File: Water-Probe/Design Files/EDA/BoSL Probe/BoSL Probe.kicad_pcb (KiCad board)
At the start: 2 copper layers, 25.4 x 12 mm, 9 parts, among them J1 8P8C_Shielded, U1 MS5803-01BA, U2 DS18B20

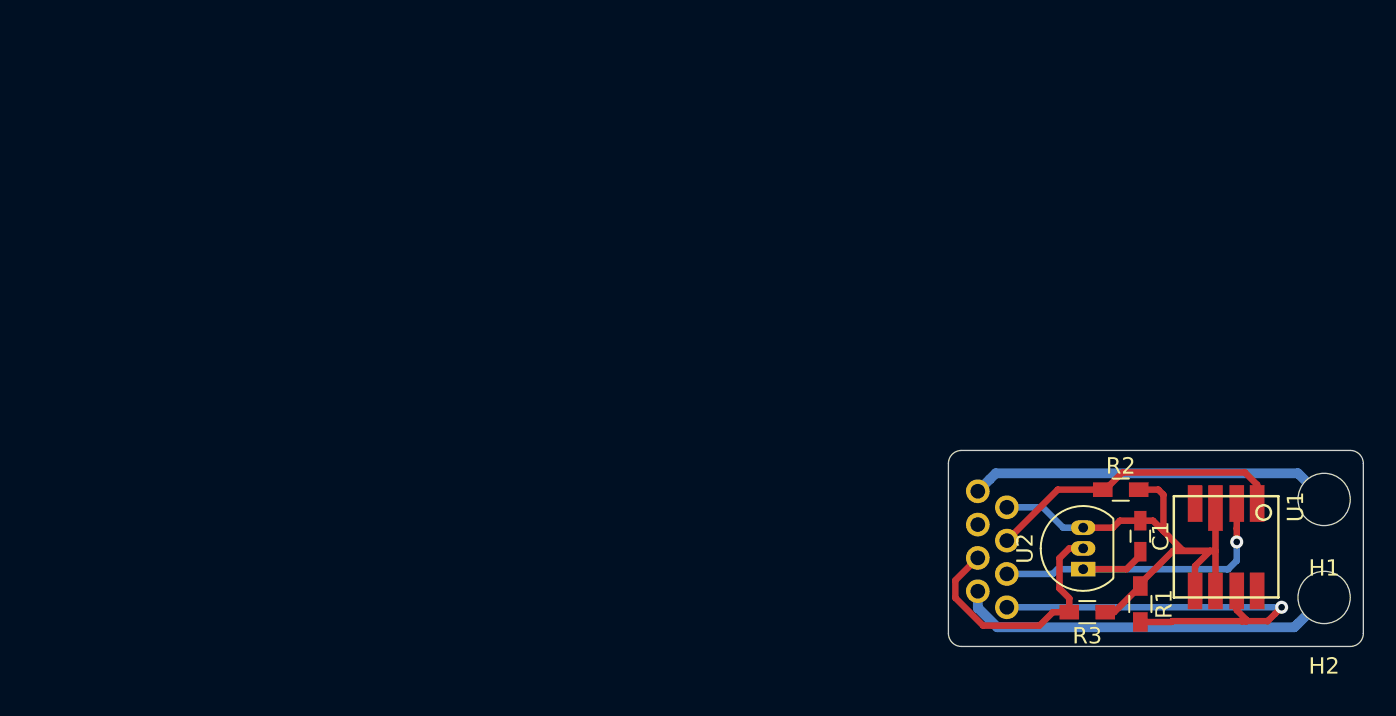
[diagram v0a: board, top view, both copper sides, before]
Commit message: finished modeling probe shape
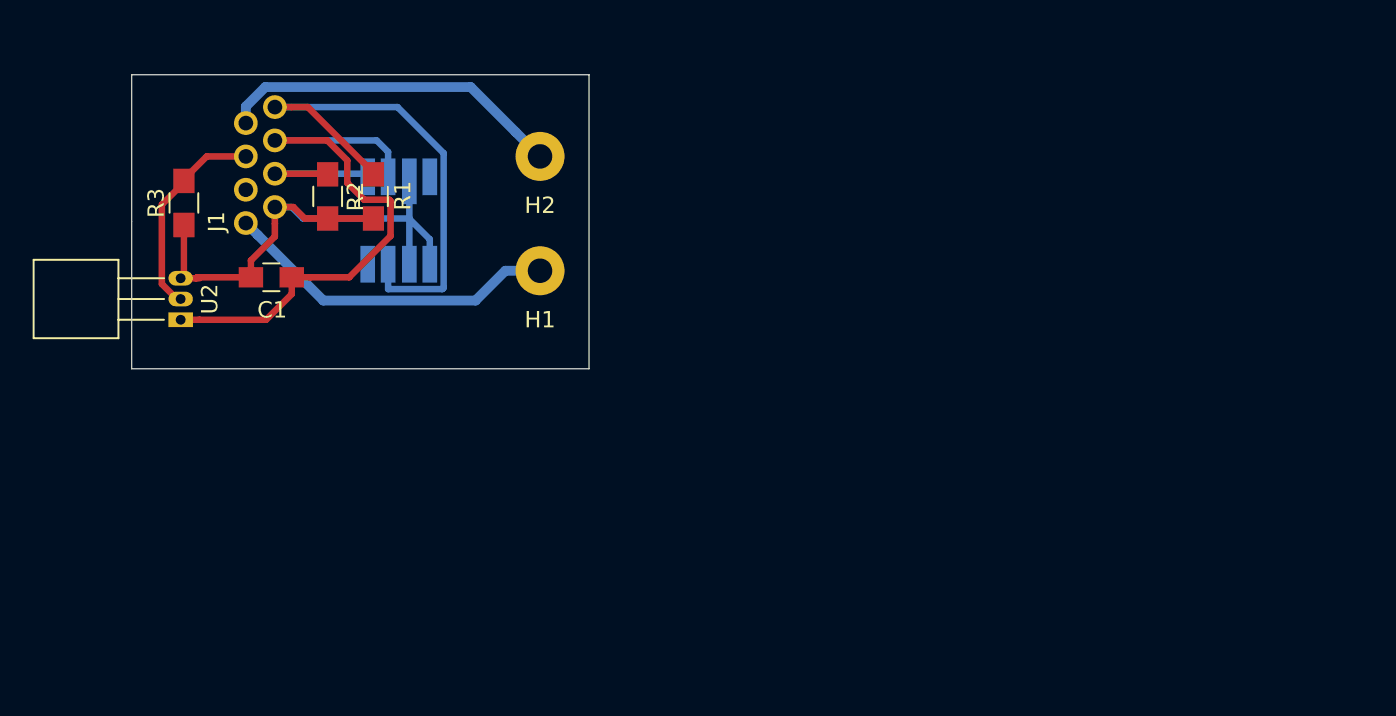
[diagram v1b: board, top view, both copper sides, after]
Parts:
- C1: footprint Capacitors_SMD:C_0603_HandSoldering -> Capacitors_SMD:C_0805_HandSoldering
- H1, H2: footprint Mounting_Holes:MountingHole_3.2mm_M3 -> Measurement_Points:Measurement_Point_Round-TH_Big
- J1: moved to F.Cu
- R1, R2, R3: footprint Resistors_SMD:R_0603_HandSoldering -> Resistors_SMD:R_0805_HandSoldering
- U1: moved to B.Cu
- U2: footprint TO_SOT_Packages_THT:TO-92_Inline_Narrow_Oval -> TO_SOT_Packages_THT:TO-92_Horizontal2_Inline_Narrow_Oval
- moved R3 60.7 mm to (103.2, 98.8), turned to 90 degrees
- moved U2 57.3 mm to (103.0, 106.0)
- moved C1 55.5 mm to (108.5, 103.4), turned to 0 degrees
- moved H2 55.1 mm to (125.0, 96.0)
- moved U1 54.5 mm to (116.3, 100.0)
- moved R1 53.2 mm to (114.8, 98.5), turned to 90 degrees
- moved R2 51.8 mm to (112.0, 98.5), turned to 270 degrees
- moved H1 50.0 mm to (125.0, 103.0)
- moved J1 47.7 mm to (107.0, 100.1), turned to 270 degrees
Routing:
- net Green: track 22.0 -> 35.9 mm, vias 1 -> 0
- net Blue: track 18.5 -> 9.01 mm
- net Brown: track 28.2 -> 32.5 mm, vias 1 -> 0
- net Orange: track 32.4 -> 36.0 mm
- net BlueHalf: track 16.4 -> 12.9 mm
- net A3: track 23.5 -> 21.3 mm
- net A0: track 22.3 -> 20.7 mm
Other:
- board size 25.4 x 12 mm -> 28 x 18 mm

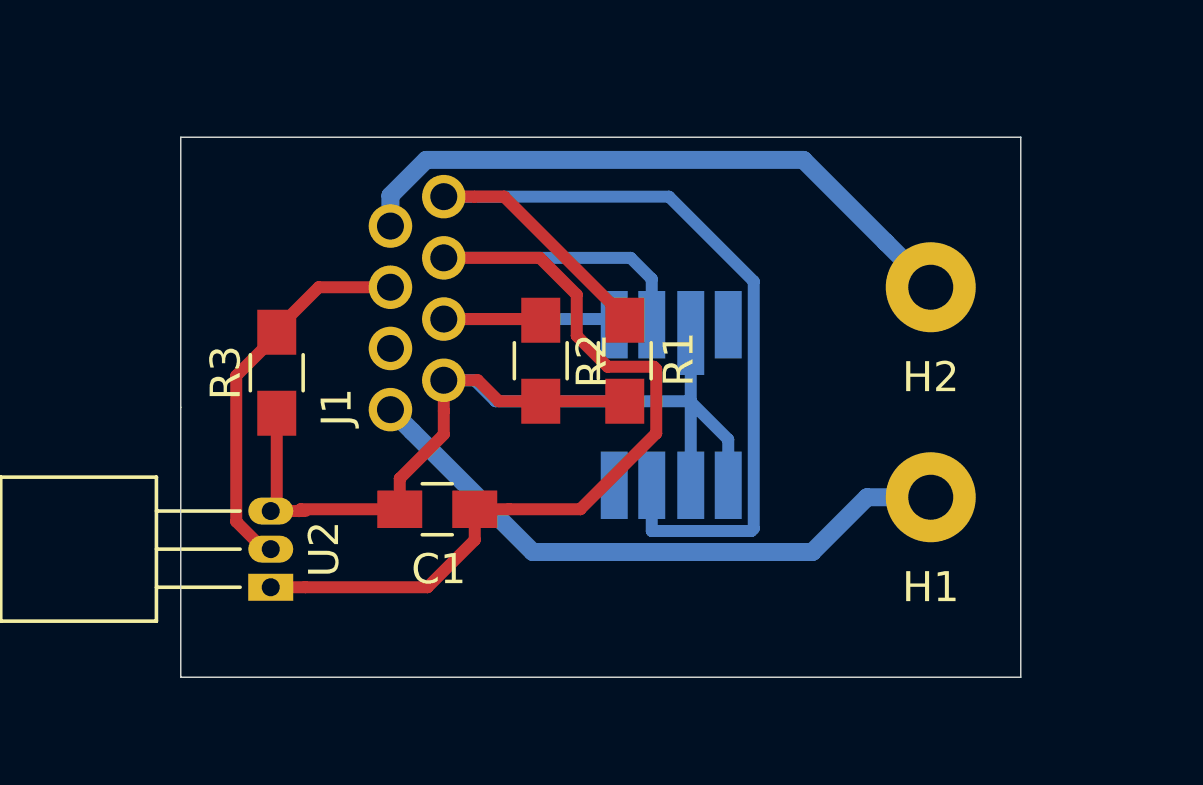
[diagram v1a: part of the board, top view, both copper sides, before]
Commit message: keystone rightangle screw connectors added
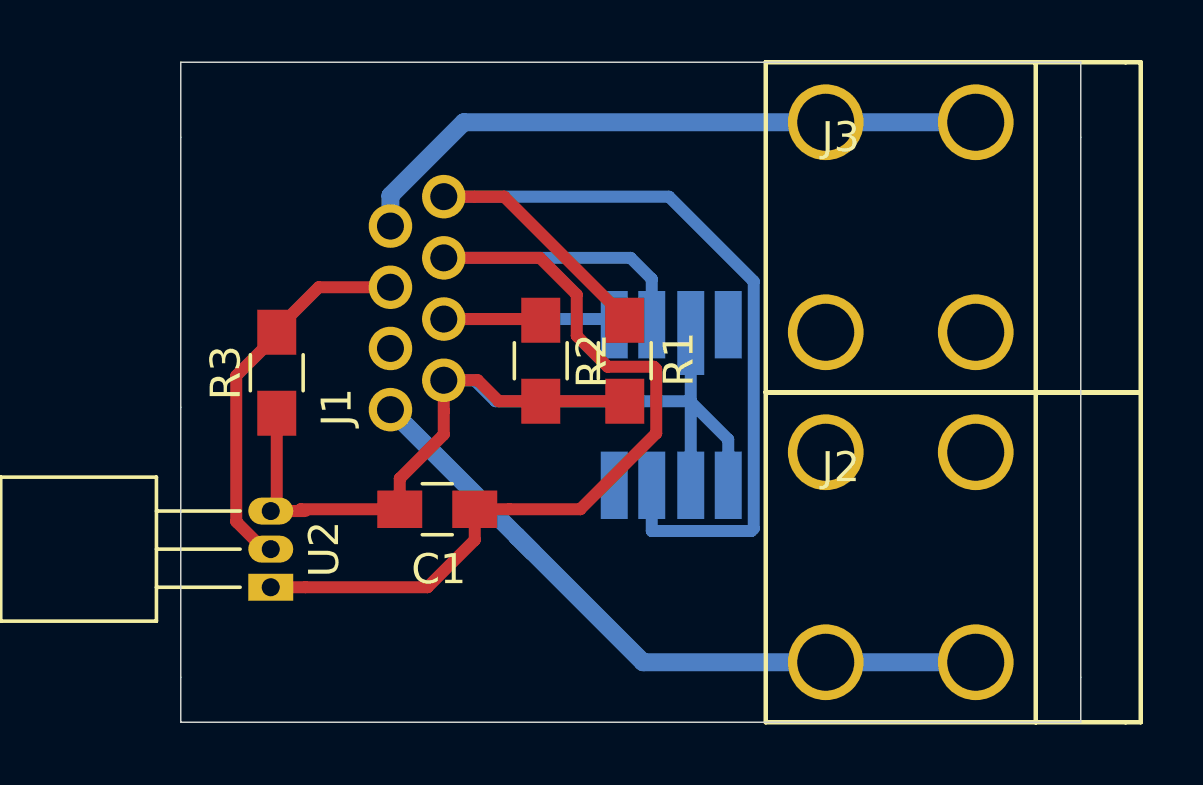
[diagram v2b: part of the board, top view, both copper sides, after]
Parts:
- removed H1, H2: MountingHole_Pad, Measurement_Points:Measurement_Point_Round-TH_Big
- added J2: KeyStone_Screw, Project:KeyStone_Screw, F.Cu at (121.5, 105.0)
- added J3: KeyStone_Screw, Project:KeyStone_Screw, F.Cu at (121.5, 94.0)
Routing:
- net A0: track 20.7 -> 23.7 mm
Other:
- board size 28 x 18 mm -> 30 x 22 mm

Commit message: commit before adding perferations to probe
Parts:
- J2, J3: value KeyStone_Screw -> KeyStone_Screw_Small; footprint Project:KeyStone_Screw -> Project:KeyStone_Screw_Small
- moved J3 1.78 mm to (122.1, 95.7)
- moved J2 0.89 mm to (122.1, 104.3)
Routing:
- net A0: track 23.7 -> 23.0 mm
- net A3: track 21.5 -> 22.1 mm
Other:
- board size 30 x 22 mm -> 29 x 18 mm
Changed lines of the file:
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@@
   (general
     (thickness 1.6)
-    (drawings 13)
-    (tracks 70)
+    (drawings 5)
+    (tracks 72)
     (zones 0)
     (modules 9)
@@
     (add_net Orange)
   )
-  (module Project:KeyStone_Screw (layer F.Cu)
-    (at 121.5 105 270)
-    (fp_text reference J2 (at -3 -0.5) (layer F.SilkS)
-      (effects (font (size 1 1) (thickness 0.15)))
-    )
-    (fp_text value KeyStone_Screw (at 4 -5.5 90) (layer F.Fab)
-      (effects (font (size 1 1) (thickness 0.15)))
-    )
-    (fp_line (start -5.5 -10.5) (end -5.5 -10) (layer F.SilkS) (width 0.15))
-    (fp_line (start 5.5 -10.5) (end -5.5 -10.5) (layer F.SilkS) (width 0.15))
-    (fp_line (start 5.5 -10) (end 5.5 -10.5) (layer F.SilkS) (width 0.15))
-    (fp_line (start -5.5 -10) (end -5.5 -7) (layer F.SilkS) (width 0.15))
-    (fp_line (start 5.5 -7) (end 5.5 -10) (layer F.SilkS) (width 0.15))
-    (fp_line (start -5.5 2) (end -5.5 -7) (layer F.SilkS) (width 0.15))
-    (fp_line (start 5.5 2) (end -5.5 2) (layer F.SilkS) (width 0.15))
-    (fp_line (start 5.5 -7) (end 5.5 2) (layer F.SilkS) (width 0.15))
-    (fp_line (start -5.5 -7) (end 5.5 -7) (layer F.SilkS) (width 0.15))
-    (pad 1 thru_hole circle (at 3.5 0 270) (size 2.524 2.524) (drill 1.9) (layers *.Cu *.Mask)
-      (net 3 A0))
-    (pad 1 thru_hole circle (at 3.5 -5 270) (size 2.524 2.524) (drill 1.9) (layers *.Cu *.Mask)
-      (net 3 A0))
-    (pad 1 thru_hole circle (at -3.5 -5 270) (size 2.524 2.524) (drill 1.9) (layers *.Cu *.Mask)
-      (net 3 A0))
-    (pad 1 thru_hole circle (at -3.5 0 270) (size 2.524 2.524) (drill 1.9) (layers *.Cu *.Mask)
-      (net 3 A0))
-  )
-  (module Project:KeyStone_Screw (layer F.Cu)
-    (at 121.5 94 270)
-    (fp_text reference J3 (at -3 -0.5) (layer F.SilkS)
-      (effects (font (size 1 1) (thickness 0.15)))
-    )
-    (fp_text value KeyStone_Screw (at 4 -5.5 90) (layer F.Fab)
-      (effects (font (size 1 1) (thickness 0.15)))
-    )
-    (fp_line (start -5.5 -10.5) (end -5.5 -10) (layer F.SilkS) (width 0.15))
-    (fp_line (start 5.5 -10.5) (end -5.5 -10.5) (layer F.SilkS) (width 0.15))
-    (fp_line (start 5.5 -10) (end 5.5 -10.5) (layer F.SilkS) (width 0.15))
-    (fp_line (start -5.5 -10) (end -5.5 -7) (layer F.SilkS) (width 0.15))
-    (fp_line (start 5.5 -7) (end 5.5 -10) (layer F.SilkS) (width 0.15))
-    (fp_line (start -5.5 2) (end -5.5 -7) (layer F.SilkS) (width 0.15))
-    (fp_line (start 5.5 2) (end -5.5 2) (layer F.SilkS) (width 0.15))
-    (fp_line (start 5.5 -7) (end 5.5 2) (layer F.SilkS) (width 0.15))
-    (fp_line (start -5.5 -7) (end 5.5 -7) (layer F.SilkS) (width 0.15))
-    (pad 1 thru_hole circle (at 3.5 0 270) (size 2.524 2.524) (drill 1.9) (layers *.Cu *.Mask)
-      (net 4 A3))
-    (pad 1 thru_hole circle (at 3.5 -5 270) (size 2.524 2.524) (drill 1.9) (layers *.Cu *.Mask)
-      (net 4 A3))
-    (pad 1 thru_hole circle (at -3.5 -5 270) (size 2.524 2.524) (drill 1.9) (layers *.Cu *.Mask)
-      (net 4 A3))
-    (pad 1 thru_hole circle (at -3.5 0 270) (size 2.524 2.524) (drill 1.9) (layers *.Cu *.Mask)
-      (net 4 A3))
-  )
   (module Project:MS5803 (layer B.Cu)
     (at 116.35 100 90)
@@
     )
   )
-  (gr_line (start 100 91) (end 100 88.5) (layer Edge.Cuts) (width 0.05))
-  (gr_line (start 100 109) (end 100 110.5) (layer Edge.Cuts) (width 0.05))
-  (gr_line (start 130 109) (end 130 110.5) (layer Edge.Cuts) (width 0.05))
-  (gr_line (start 130 88.5) (end 130 91) (layer Edge.Cuts) (width 0.05))
-  (gr_line (start 130 91) (end 130 109) (layer Edge.Cuts) (width 0.05))
-  (gr_line (start 100 110.5) (end 130 110.5) (layer Edge.Cuts) (width 0.05))
+  (module Project:KeyStone_Screw_Small (layer F.Cu)
+    (at 122.08 104.32 270)
+    (fp_text reference J2 (at -1 -8 90) (layer F.SilkS)
+      (effects (font (size 1 1) (thickness 0.15)))
+    )
+    (fp_text value KeyStone_Screw_Small (at -1 -2 90) (layer F.Fab)
+      (effects (font (size 1 1) (thickness 0.15)))
+    )
+    (fp_line (start -3.92 -9) (end 3.92 -9) (layer F.SilkS) (width 0.15))
+    (fp_line (start -3.92 -7) (end 3.92 -7) (layer F.SilkS) (width 0.15))
+    (fp_line (start -3.92 1.3) (end 3.92 1.3) (layer F.SilkS) (width 0.15))
+    (fp_line (start -3.92 -7) (end -3.92 -9) (layer F.SilkS) (width 0.15))
+    (fp_line (start 3.92 -7) (end 3.92 -9) (layer F.SilkS) (width 0.15))
+    (fp_line (start -3.92 -7) (end -3.92 1.3) (layer F.SilkS) (width 0.15))
+    (fp_line (start 3.92 -7) (end 3.92 1.3) (layer F.SilkS) (width 0.15))
+    (pad 1 thru_hole circle (at 2.72 0.08) (size 2.2 2.2) (drill 1.7) (layers *.Cu *.Mask)
+      (net 3 A0))
+    (pad 1 thru_hole circle (at 2.72 -5 270) (size 2.2 2.2) (drill 1.7) (layers *.Cu *.Mask)
+      (net 3 A0))
+    (pad 1 thru_hole circle (at -2.72 0.08) (size 2.2 2.2) (drill 1.7) (layers *.Cu *.Mask)
+      (net 3 A0))
+    (pad 1 thru_hole circle (at -2.72 -5 270) (size 2.2 2.2) (drill 1.7) (layers *.Cu *.Mask)
+      (net 3 A0))
+    (model "D:/data/My Documents/Monash/Monash-BoSL/Water-Probe/Design Files/CAD/Parts/Keystone_Screw_Small.wrl"
+      (at (xyz 0 0 0))
+      (scale (xyz 1 1 1))
+      (rotate (xyz 0 0 0))
+    )
+  )
+  (module Project:KeyStone_Screw_Small (layer F.Cu)
+    (at 122.08 95.68 270)
+    (fp_text reference J3 (at -1 -8 90) (layer F.SilkS)
+      (effects (font (size 1 1) (thickness 0.15)))
+    )
+    (fp_text value KeyStone_Screw_Small (at -1 -2 90) (layer F.Fab)
+      (effects (font (size 1 1) (thickness 0.15)))
+    )
+    (fp_line (start 3.92 -7) (end 3.92 1.3) (layer F.SilkS) (width 0.15))
+    (fp_line (start -3.92 -7) (end -3.92 1.3) (layer F.SilkS) (width 0.15))
+    (fp_line (start 3.92 -7) (end 3.92 -9) (layer F.SilkS) (width 0.15))
+    (fp_line (start -3.92 -7) (end -3.92 -9) (layer F.SilkS) (width 0.15))
+    (fp_line (start -3.92 1.3) (end 3.92 1.3) (layer F.SilkS) (width 0.15))
+    (fp_line (start -3.92 -7) (end 3.92 -7) (layer F.SilkS) (width 0.15))
+    (fp_line (start -3.92 -9) (end 3.92 -9) (layer F.SilkS) (width 0.15))
+    (pad 1 thru_hole circle (at -2.72 -5 270) (size 2.2 2.2) (drill 1.7) (layers *.Cu *.Mask)
+      (net 4 A3))
+    (pad 1 thru_hole circle (at -2.72 0.08) (size 2.2 2.2) (drill 1.7) (layers *.Cu *.Mask)
+      (net 4 A3))
+    (pad 1 thru_hole circle (at 2.72 -5 270) (size 2.2 2.2) (drill 1.7) (layers *.Cu *.Mask)
+      (net 4 A3))
+    (pad 1 thru_hole circle (at 2.72 0.08) (size 2.2 2.2) (drill 1.7) (layers *.Cu *.Mask)
+      (net 4 A3))
+    (model "D:/data/My Documents/Monash/Monash-BoSL/Water-Probe/Design Files/CAD/Parts/Keystone_Screw_Small.wrl"
+      (at (xyz 0 0 0))
+      (scale (xyz 1 1 1))
+      (rotate (xyz 0 0 0))
+    )
+  )
+  (gr_line (start 129 91) (end 129 109) (layer Edge.Cuts) (width 0.05))
+  (gr_line (start 100 109) (end 129 109) (layer Edge.Cuts) (width 0.05))
   (gr_line (start 100 100) (end 100 109) (layer Edge.Cuts) (width 0.05))
-  (gr_line (start 100 88.5) (end 130 88.5) (layer Edge.Cuts) (width 0.05))
+  (gr_line (start 100 91) (end 129 91) (layer Edge.Cuts) (width 0.05))
   (gr_line (start 100 100) (end 100 91) (layer Edge.Cuts) (width 0.05))
-  (gr_line (start 100 100) (end 50 100) (layer F.Mask) (width 0.15))
-  (gr_line (start 100 100) (end 165 100) (layer F.Mask) (width 0.15))
-  (gr_line (start 100 100) (end 100 140) (layer F.Mask) (width 0.15))
-  (gr_line (start 100 100) (end 100 65) (layer F.Mask) (width 0.15))
   (segment (start 115.7 95.725) (end 115.7 97.25) (width 0.4) (layer B.Cu) (net 1) (status 20))
   (segment (start 114.995 95.02) (end 115.7 95.725) (width 0.4) (layer B.Cu) (net 1))
@@
   (segment (start 103.2 100.2) (end 103.2 103.26) (width 0.4) (layer F.Cu) (net 2) (status 30))
   (segment (start 114.8 99.8) (end 112 99.8) (width 0.4) (layer F.Cu) (net 2) (status 30))
-  (segment (start 115.41 108.5) (end 111.205 104.295) (width 0.6) (layer B.Cu) (net 3))
-  (segment (start 121.5 108.5) (end 115.41 108.5) (width 0.6) (layer B.Cu) (net 3))
-  (segment (start 106.99 100.08) (end 111.205 104.295) (width 0.6) (layer B.Cu) (net 3))
-  (segment (start 111.205 104.295) (end 111.735009 104.825009) (width 0.6) (layer B.Cu) (net 3))
-  (segment (start 121.5 108.5) (end 126.5 108.5) (width 0.6) (layer B.Cu) (net 3))
-  (segment (start 109.434998 90.5) (end 121.5 90.5) (width 0.6) (layer B.Cu) (net 4))
+  (segment (start 111.205 104.295) (end 106.99 100.08) (width 0.6) (layer B.Cu) (net 3))
+  (segment (start 111.91 105) (end 111.205 104.295) (width 0.6) (layer B.Cu) (net 3))
+  (segment (start 122 107.04) (end 119.96 105) (width 0.6) (layer B.Cu) (net 3))
+  (segment (start 119.96 105) (end 111.91 105) (width 0.6) (layer B.Cu) (net 3))
+  (segment (start 122 107.04) (end 127.08 107.04) (width 0.6) (layer B.Cu) (net 3))
+  (segment (start 120.900001 91.860001) (end 122 92.96) (width 0.6) (layer B.Cu) (net 4))
+  (segment (start 120.794999 91.754999) (end 120.900001 91.860001) (width 0.6) (layer B.Cu) (net 4))
+  (segment (start 108.179999 91.754999) (end 120.794999 91.754999) (width 0.6) (layer B.Cu) (net 4))
+  (segment (start 106.99 92.944998) (end 108.179999 91.754999) (width 0.6) (layer B.Cu) (net 4))
   (segment (start 106.99 93.96) (end 106.99 92.944998) (width 0.6) (layer B.Cu) (net 4))
-  (segment (start 106.99 92.944998) (end 109.434998 90.5) (width 0.6) (layer B.Cu) (net 4))
-  (segment (start 121.5 90.5) (end 126.5 90.5) (width 0.6) (layer B.Cu) (net 4))
+  (segment (start 122 92.96) (end 127.08 92.96) (width 0.6) (layer B.Cu) (net 4))
   (segment (start 114.26 97.06) (end 114.45 97.25) (width 0.4) (layer B.Cu) (net 5) (status 30))
   (segment (start 108.768 97.06) (end 114.26 97.06) (width 0.4) (layer B.Cu) (net 5) (status 30))
